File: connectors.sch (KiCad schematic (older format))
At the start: 27 parts, among them J1 2001-1-2-21-00-BK, J2 JC-128, P2 HOST, P3 CAM1, P4 CONN_02X20, Q3 2N7002P.215

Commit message: Added datasheet links to BOM
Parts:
- J1: Category Connectors, Interconnects -> (none); DK_Datasheet_Link http://cnctech.us/pdfs/2001-1-2-21-00-BK.pdf -> (none); DK_Detail_Page /product-detail/en/cnc-tech/2001-1-2-21-00-BK/1175-1704-1-N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 -> (none); Description CONN RCPT MINI HDMI 19POS SMD RA -> (none); Digi-Key_PN 1175-1704-1-ND -> (none); Family USB, DVI, HDMI Connectors -> (none); MPN 2001-1-2-21-00-BK -> (none); Manufacturer CNC Tech -> (none); Status Active -> (none)
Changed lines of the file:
@@
 F 1 "CAM1" V 2200 1700 50  0000 C CNN
 F 2 "ffc_conn:FPC_22" H 2100 1700 50  0001 C CNN
-F 3 "" H 2100 1700 50  0000 C CNN
+F 3 "https://gr.mouser.com/datasheet/2/445/687122183722-1114273.pdf" H 2100 1700 50  0001 C CNN
 	1    2100 1700
 	-1   0    0    -1
@@
 F 1 "HOST" H 1200 1000 50  0000 C CNN
 F 2 "Connectors:USB_A" V 1200 700 50  0001 C CNN
-F 3 "" V 1200 700 50  0000 C CNN
+F 3 "https://gr.mouser.com/datasheet/2/643/bel_SS-52100-001-1216592.pdf" V 1200 700 50  0001 C CNN
 	1    1250 800
 	1    0    0    -1
@@
 F 1 "2001-1-2-21-00-BK" V 5860 1095 60  0000 C CNN
 F 2 "HDMI_MOLEX:HDMI_MOLEX_471510001" H 6450 2250 60  0001 L CNN
-F 3 "http://cnctech.us/pdfs/2001-1-2-21-00-BK.pdf" H 6450 2350 60  0001 L CNN
-F 4 "1175-1704-1-ND" H 6450 2450 60  0001 L CNN "Digi-Key_PN"
-F 5 "2001-1-2-21-00-BK" H 6450 2550 60  0001 L CNN "MPN"
-F 6 "Connectors, Interconnects" H 6450 2650 60  0001 L CNN "Category"
-F 7 "USB, DVI, HDMI Connectors" H 6450 2750 60  0001 L CNN "Family"
-F 8 "http://cnctech.us/pdfs/2001-1-2-21-00-BK.pdf" H 6450 2850 60  0001 L CNN "DK_Datasheet_Link"
-F 9 "/product-detail/en/cnc-tech/2001-1-2-21-00-BK/1175-1704-1-ND/4867013" H 6450 2950 60  0001 L CNN "DK_Detail_Page"
-F 10 "CONN RCPT MINI HDMI 19POS SMD RA" H 6450 3050 60  0001 L CNN "Description"
-F 11 "CNC Tech" H 6450 3150 60  0001 L CNN "Manufacturer"
-F 12 "Active" H 6450 3250 60  0001 L CNN "Status"
+F 3 "https://gr.mouser.com/datasheet/2/276/0471510001_IO_CONNECTORS-170105.pdf" H 6450 2350 60  0001 L CNN
 	1    6250 2050
 	1    0    0    -1
@@
 F 1 "BAV99" H 8400 3550 50  0000 C CNN
 F 2 "TO_SOT_Packages_SMD:SOT-23" H 8400 3450 50  0001 C CNN
-F 3 "" H 8400 3450 50  0000 C CNN
+F 3 "https://gr.mouser.com/datasheet/2/427/bav99g-266615.pdf" H 8400 3450 50  0001 C CNN
 	1    8400 3450
 	0    1    -1   0
@@
 F 1 "BAV99" H 8900 3550 50  0000 C CNN
 F 2 "TO_SOT_Packages_SMD:SOT-23" H 8900 3450 50  0001 C CNN
-F 3 "" H 8900 3450 50  0000 C CNN
+F 3 "https://gr.mouser.com/datasheet/2/427/bav99g-266615.pdf" H 8900 3450 50  0001 C CNN
 	1    8900 3450
 	0    1    -1   0
@@
 F 1 "BAV99" H 9400 3550 50  0000 C CNN
 F 2 "TO_SOT_Packages_SMD:SOT-23" H 9400 3450 50  0001 C CNN
-F 3 "" H 9400 3450 50  0000 C CNN
+F 3 "https://gr.mouser.com/datasheet/2/427/bav99g-266615.pdf" H 9400 3450 50  0001 C CNN
 	1    9400 3450
 	0    1    -1   0
@@
 F 1 "2N7002P.215" H 10600 3400 50  0000 L CNN
 F 2 "TO_SOT_Packages_SMD:SOT-23" H 10600 3550 50  0001 C CNN
-F 3 "" H 10400 3450 50  0000 C CNN
+F 3 "https://www.tme.eu/en/Document/fda24b70d66290936384ff869f03745e/2N7002P.pdf" H 10400 3450 50  0001 C CNN
 	1    10400 3450
 	1    0    0    -1
@@
 F 1 "BAV99" H 9900 3550 50  0000 C CNN
 F 2 "TO_SOT_Packages_SMD:SOT-23" H 9900 3450 50  0001 C CNN
-F 3 "" H 9900 3450 50  0000 C CNN
+F 3 "https://gr.mouser.com/datasheet/2/427/bav99g-266615.pdf" H 9900 3450 50  0001 C CNN
 	1    9900 3450
 	0    1    -1   0
@@
 F 1 "BAT54" H 7800 1500 50  0000 C CNN
 F 2 "TO_SOT_Packages_SMD:SOT-23" H 7800 1600 50  0001 C CNN
-F 3 "" H 7800 1600 50  0000 C CNN
+F 3 "https://gr.mouser.com/datasheet/2/427/bat54-58352.pdf" H 7800 1600 50  0001 C CNN
 	1    7800 1600
 	0    -1   -1   0
@@
 F 1 "BAT54" H 650 850 50  0000 C CNN
 F 2 "TO_SOT_Packages_SMD:SOT-23" H 650 950 50  0001 C CNN
-F 3 "" H 650 950 50  0000 C CNN
+F 3 "https://gr.mouser.com/datasheet/2/427/bat54-58352.pdf" H 650 950 50  0001 C CNN
 	1    650  950
 	0    -1   -1   0
@@
 F 1 "BAV99" H 1900 5000 50  0000 C CNN
 F 2 "TO_SOT_Packages_SMD:SOT-23" H 1900 4900 50  0001 C CNN
-F 3 "" H 1900 4900 50  0000 C CNN
+F 3 "https://gr.mouser.com/datasheet/2/427/bav99g-266615.pdf" H 1900 4900 50  0001 C CNN
 	1    1900 4900
 	0    1    -1   0
@@
 F 1 "BAV99" H 2400 5000 50  0000 C CNN
 F 2 "TO_SOT_Packages_SMD:SOT-23" H 2400 4900 50  0001 C CNN
-F 3 "" H 2400 4900 50  0000 C CNN
+F 3 "https://gr.mouser.com/datasheet/2/427/bav99g-266615.pdf" H 2400 4900 50  0001 C CNN
 	1    2400 4900
 	0    1    -1   0
@@
 F 1 "JC-128" H 950 3900 50  0000 C CNN
 F 2 "jc-128:JC-128" H 1100 4000 50  0001 C CNN
-F 3 "" H 1100 4000 50  0000 C CNN
+F 3 "https://www.tme.eu/en/Document/b2d3db3ed78affad83450dce59a7cdd9/jc-128.pdf" H 1100 4000 50  0001 C CNN
 	1    1000 4200
 	1    0    0    -1

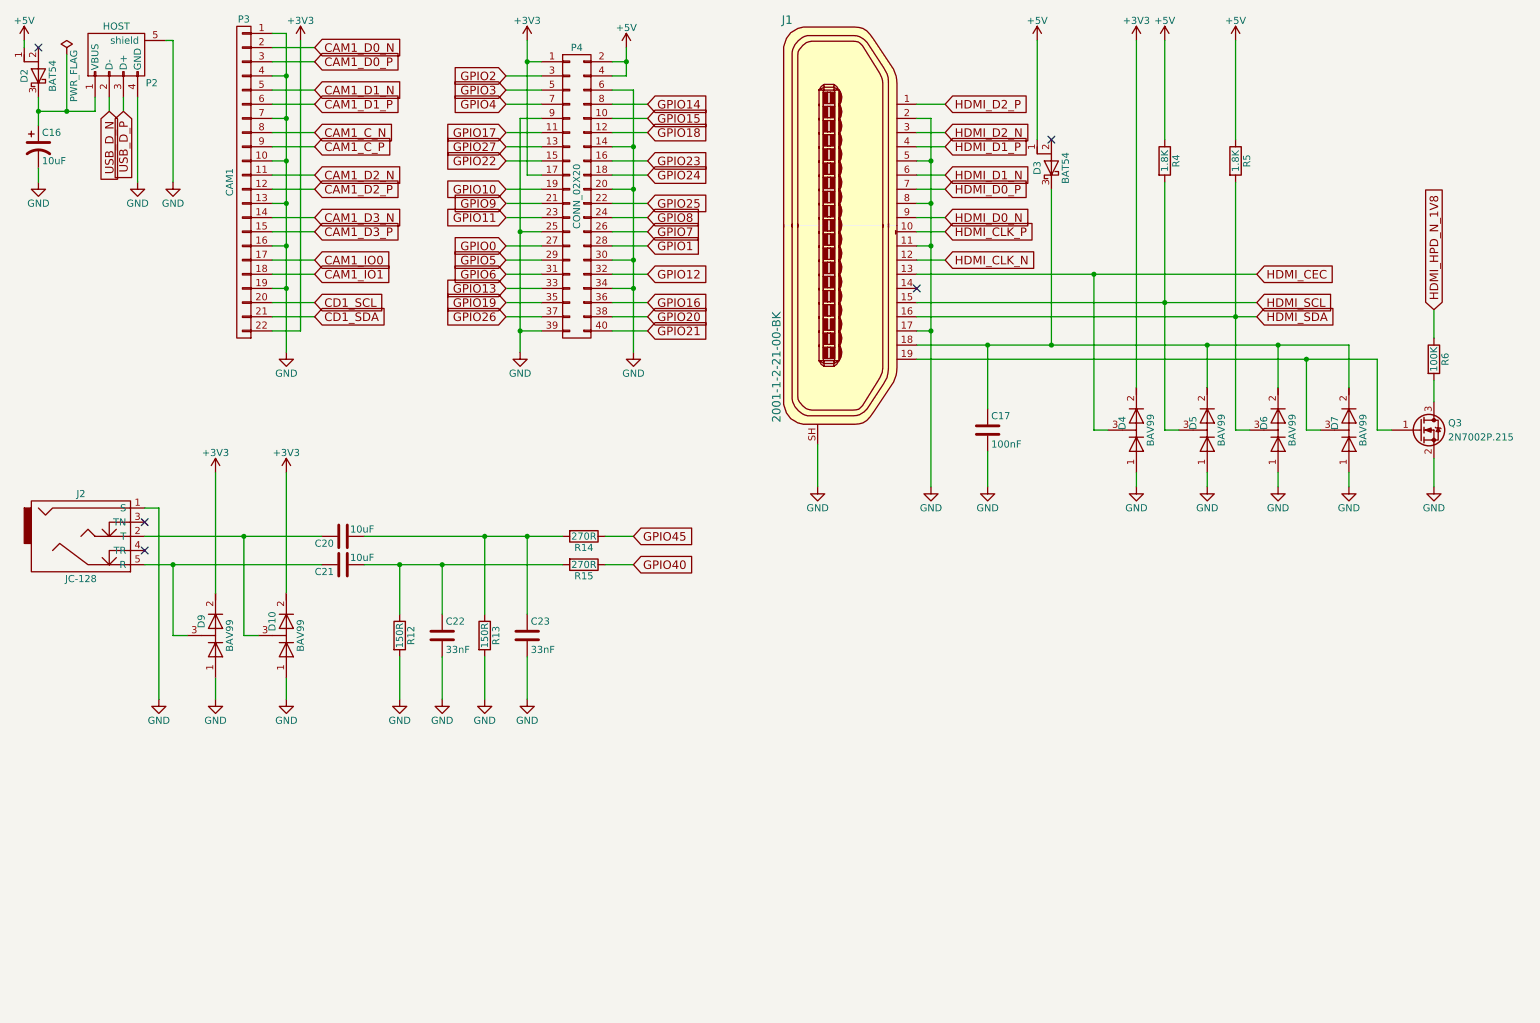
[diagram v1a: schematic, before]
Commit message: Schematic changes to support CAM0
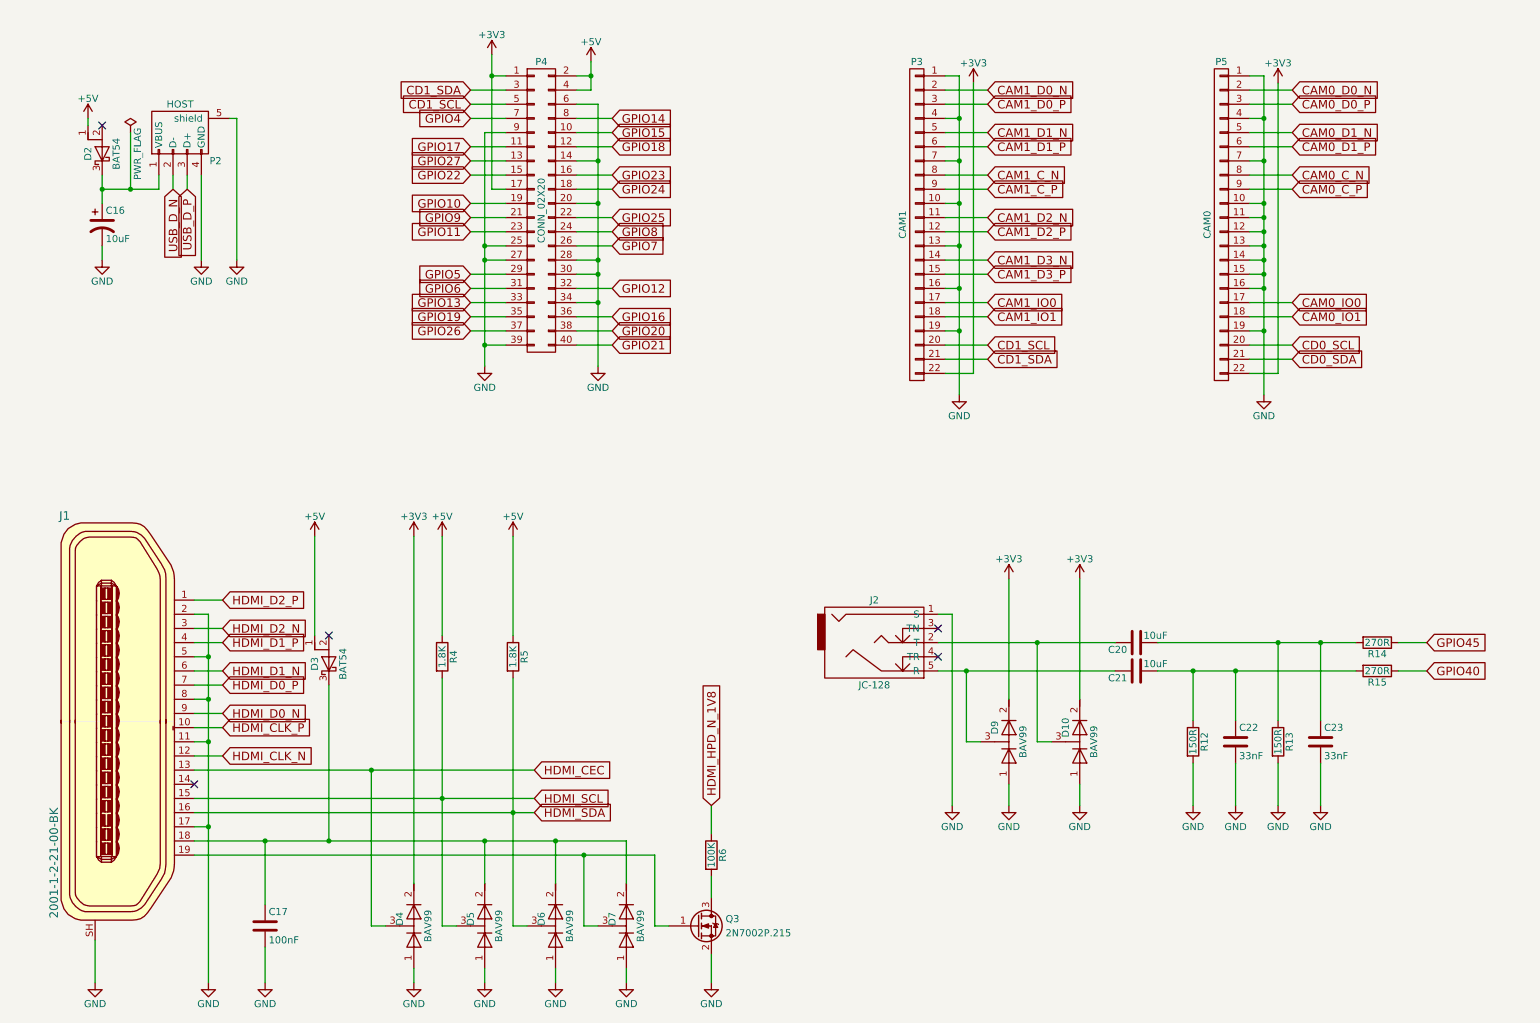
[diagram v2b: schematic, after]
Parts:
- added P5: CAM0, ffc_conn:FPC_22, symbol CONN_01X22
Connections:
- net GPIO0 is gone; now on net GND: P4.27 (P27)
- net GPIO1 is gone; now on net GND: P4.28 (P28)
- net GPIO2 is gone; now on net CD1_SDA: P4.3 (P3)
- net GPIO3 is gone; now on net CD1_SCL: P4.5 (P5)
- net +3V3: now also P5.22 (P22)
- net GND: now also P5.1 (P1), P5.10 (P10), P5.11 (P11), P5.12 (P12), P5.13 (P13), P5.14 (P14), P5.15 (P15), P5.16 (P16), P5.19 (P19), P5.4 (P4), P5.7 (P7)
- new net CAM0_C_N: P5.8 (P8)
- new net CAM0_C_P: P5.9 (P9)
- new net CAM0_D0_N: P5.2 (P2)
- new net CAM0_D0_P: P5.3 (P3)
- new net CAM0_D1_N: P5.5 (P5)
- new net CAM0_D1_P: P5.6 (P6)
- new net CAM0_IO0: P5.17 (P17)
- new net CAM0_IO1: P5.18 (P18)
- new net CD0_SCL: P5.20 (P20)
- new net CD0_SDA: P5.21 (P21)
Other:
- moved on the sheet: C16, C17, C20, C21, C22, C23, D10, D2, D3, D4, D5, D6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

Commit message: Initial PCB changes to support CAM0+CAM1
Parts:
- P2: symbol USB_A -> USB_A-RESCUE-compute_module
